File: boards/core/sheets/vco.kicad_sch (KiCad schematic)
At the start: 53 parts, among them Q201 2N3906, Q202 BC847BS, Q206 MMBFJ111, Q301 MMBT5551, U201 TL072, U202 TL072, U206 LM311

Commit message: Added schematics docs
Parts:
- renumbered C274 to C273, Q206 to Q203, R323 to R322, R325 to R324, R327 to R326, R331 to R330, TH204 to TH203, TP205 to TP201, TP206 to TP202, TP207 to TP203, TP208 to TP204, TP234 to TP233, U206 to U203
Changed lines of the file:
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@@
 		(dnp no)
 		(fields_autoplaced yes)
-		(property "Reference" "#PWR0381"
+		(property "Reference" "#PWR0380"
 			(at 43.18 87.63 0)
 			(effects
@@
 		(on_board yes)
 		(dnp no)
-		(property "Reference" "TP208"
+		(property "Reference" "TP204"
 			(at 279.4 46.99 90)
 			(effects
@@
 		(dnp no)
 		(fields_autoplaced yes)
-		(property "Reference" "C274"
+		(property "Reference" "C273"
 			(at 269.24 128.27 90)
 			(effects
@@
 		(dnp no)
 		(fields_autoplaced yes)
-		(property "Reference" "R325"
+		(property "Reference" "R324"
 			(at 237.49 144.78 0)
 			(effects
@@
 		(on_board yes)
 		(dnp no)
-		(property "Reference" "TP206"
+		(property "Reference" "TP202"
 			(at 158.115 134.62 90)
 			(effects
@@
 		(dnp no)
 		(fields_autoplaced yes)
-		(property "Reference" "#PWR0389"
+		(property "Reference" "#PWR0388"
 			(at 234.95 163.83 0)
 			(effects
@@
 		(on_board yes)
 		(dnp no)
-		(property "Reference" "TP207"
+		(property "Reference" "TP203"
 			(at 235.585 91.44 90)
 			(effects
@@
 		(on_board yes)
 		(dnp no)
-		(property "Reference" "U206"
+		(property "Reference" "U203"
 			(at 266.7 63.5 0)
 			(effects
@@
 		(dnp no)
 		(fields_autoplaced yes)
-		(property "Reference" "#PWR0385"
+		(property "Reference" "#PWR0384"
 			(at 219.71 154.94 0)
 			(effects
@@
 		(on_board yes)
 		(dnp no)
-		(property "Reference" "TP205"
+		(property "Reference" "TP201"
 			(at 148.59 57.15 0)
 			(effects
@@
 		(dnp no)
 		(fields_autoplaced yes)
-		(property "Reference" "#PWR0387"
+		(property "Reference" "#PWR0386"
 			(at 228.6 148.59 0)
 			(effects
@@
 		(dnp no)
 		(fields_autoplaced yes)
-		(property "Reference" "#PWR0383"
+		(property "Reference" "#PWR0382"
 			(at 43.18 96.52 0)
 			(effects
@@
 		(dnp no)
 		(fields_autoplaced yes)
-		(property "Reference" "#PWR0393"
+		(property "Reference" "#PWR0392"
 			(at 288.29 153.67 0)
 			(effects
@@
 		(dnp no)
 		(fields_autoplaced yes)
-		(property "Reference" "R327"
+		(property "Reference" "R326"
 			(at 237.49 154.94 0)
 			(effects
@@
 		(dnp no)
 		(fields_autoplaced yes)
-		(property "Reference" "TH204"
+		(property "Reference" "TH203"
 			(at 117.1575 71.12 90)
 			(effects
@@
 		(dnp no)
 		(fields_autoplaced yes)
-		(property "Reference" "#PWR0241"
+		(property "Reference" "#PWR0224"
 			(at 246.38 105.41 0)
 			(effects
@@
 		(dnp no)
 		(fields_autoplaced yes)
-		(property "Reference" "#PWR0391"
+		(property "Reference" "#PWR0390"
 			(at 274.32 153.67 0)
 			(effects
@@
 		(dnp no)
 		(fields_autoplaced yes)
-		(property "Reference" "#PWR0370"
+		(property "Reference" "#PWR0369"
 			(at 111.76 134.62 0)
 			(effects
@@
 		(dnp no)
 		(fields_autoplaced yes)
-		(property "Reference" "Q206"
+		(property "Reference" "Q203"
 			(at 224.79 41.91 90)
 			(effects
@@
 		(dnp no)
 		(fields_autoplaced yes)
-		(property "Reference" "R323"
+		(property "Reference" "R322"
 			(at 222.25 138.43 0)
 			(effects
@@
 		(dnp no)
 		(fields_autoplaced yes)
-		(property "Reference" "#PWR0244"
+		(property "Reference" "#PWR0227"
 			(at 271.78 83.82 0)
 			(effects
@@
 		(dnp no)
 		(fields_autoplaced yes)
-		(property "Reference" "R331"
+		(property "Reference" "R330"
 			(at 290.83 140.97 0)
 			(effects
@@
 		(on_board yes)
 		(dnp no)
-		(property "Reference" "TP234"
+		(property "Reference" "TP233"
 			(at 226.695 72.39 90)
 			(effects
@@
 		(dnp no)
 		(fields_autoplaced yes)
-		(property "Reference" "#PWR0240"
+		(property "Reference" "#PWR0223"
 			(at 246.38 82.55 0)
 			(effects
@@
 		(dnp no)
 		(fields_autoplaced yes)
-		(property "Reference" "#PWR0395"
+		(property "Reference" "#PWR0394"
 			(at 299.72 153.67 0)
 			(effects

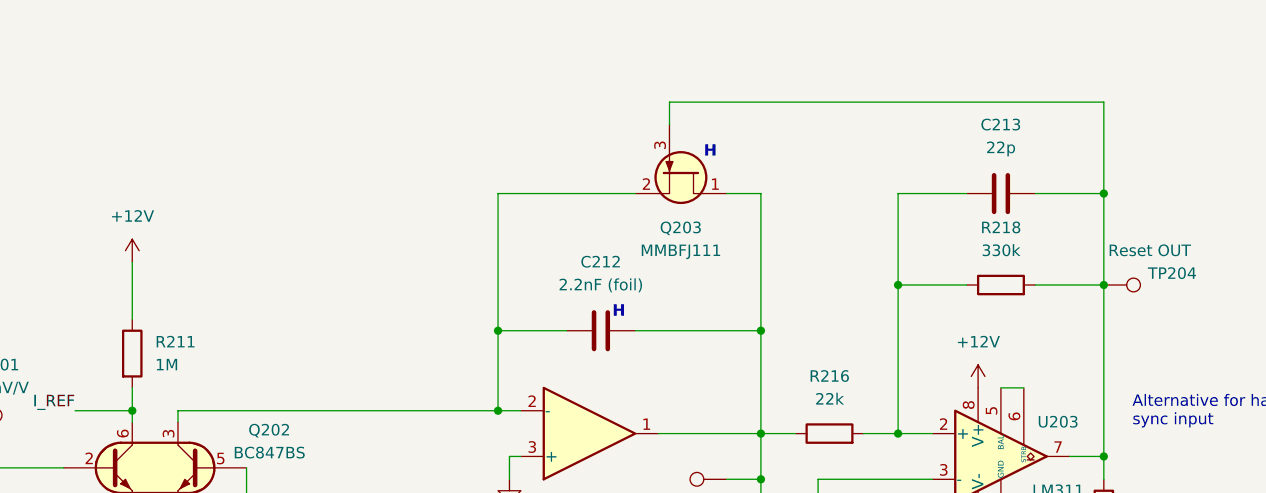
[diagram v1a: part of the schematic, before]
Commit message: Added THT footprint to J111 in VCOs
https://github.com/shmoergh/hog/issues/10
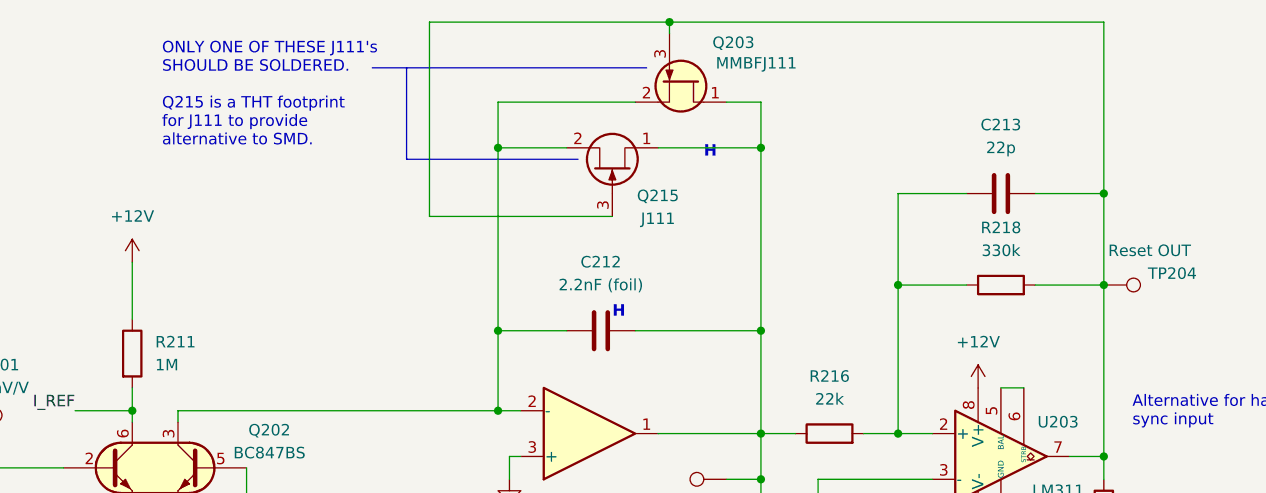
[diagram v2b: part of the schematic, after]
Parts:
- added Q215: J111, Package_TO_SOT_THT:TO-92_Inline_Wide, symbol Transistor_FET:MMBFJ111
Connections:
- net RAW_SAW: now also Q215.1 (D)
- net at C213.2, Q203.3 (G), R218.2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: now also Q215.3 (G)
- net at C212.1, Q202.3 (C2), Q203.2 (S)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: now also Q215.2 (S)
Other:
- note added: "ONLY ONE OF THESE J111's SHOULD BE SOLDERED. Q215 is a THT footprint for J111 to provide alternative to SMD."
- moved on the sheet: Q203
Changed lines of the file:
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@@
 	)
 	(junction
+		(at 223.52 19.05)
+		(diameter 0)
+		(color 0 0 0 0)
+	)
+	(junction
 		(at 60.96 66.04)
 		(diameter 0)
@@
 	)
 	(junction
+		(at 233.68 33.02)
+		(diameter 0)
+		(color 0 0 0 0)
+	)
+	(junction
 		(at 148.59 68.58)
 		(diameter 0)
@@
 	)
 	(junction
+		(at 204.47 33.02)
+		(diameter 0)
+		(color 0 0 0 0)
+	)
+	(junction
 		(at 288.29 135.89)
 		(diameter 0)
@@
 	(wire
 		(pts
-			(xy 233.68 38.1) (xy 233.68 53.34)
+			(xy 233.68 27.94) (xy 233.68 33.02)
 		)
 		(stroke
@@
 		)
 	)
+	(polyline
+		(pts
+			(xy 190.5 24.13) (xy 220.98 24.13)
+		)
+		(stroke
+			(width 0)
+			(type default)
+		)
+	)
 	(wire
 		(pts
@@
 	(wire
 		(pts
+			(xy 222.25 33.02) (xy 233.68 33.02)
+		)
+		(stroke
+			(width 0)
+			(type default)
+		)
+	)
+	(wire
+		(pts
 			(xy 128.27 128.27) (xy 128.27 130.81)
 		)
@@
 	(wire
 		(pts
+			(xy 196.85 40.64) (xy 196.85 19.05)
+		)
+		(stroke
+			(width 0)
+			(type default)
+		)
+	)
+	(wire
+		(pts
 			(xy 161.29 132.08) (xy 166.37 132.08)
 		)
@@
 	(wire
 		(pts
+			(xy 204.47 33.02) (xy 204.47 53.34)
+		)
+		(stroke
+			(width 0)
+			(type default)
+		)
+	)
+	(wire
+		(pts
 			(xy 233.68 69.85) (xy 233.68 81.28)
 		)
@@
 		)
 	)
+	(polyline
+		(pts
+			(xy 194.31 34.29) (xy 213.36 34.29)
+		)
+		(stroke
+			(width 0)
+			(type default)
+		)
+	)
 	(wire
 		(pts
@@
 	(wire
 		(pts
-			(xy 204.47 38.1) (xy 219.71 38.1)
+			(xy 204.47 27.94) (xy 219.71 27.94)
 		)
 		(stroke
@@
 		)
 	)
+	(polyline
+		(pts
+			(xy 194.31 24.13) (xy 194.31 34.29)
+		)
+		(stroke
+			(width 0)
+			(type default)
+		)
+	)
 	(wire
 		(pts
@@
 	(wire
 		(pts
-			(xy 223.52 27.94) (xy 223.52 30.48)
+			(xy 223.52 19.05) (xy 223.52 20.32)
 		)
 		(stroke
@@
 	(wire
 		(pts
+			(xy 217.17 40.64) (xy 196.85 40.64)
+		)
+		(stroke
+			(width 0)
+			(type default)
+		)
+	)
+	(wire
+		(pts
 			(xy 148.59 114.3) (xy 148.59 125.73)
 		)
@@
 	(wire
 		(pts
-			(xy 229.87 38.1) (xy 233.68 38.1)
+			(xy 229.87 27.94) (xy 233.68 27.94)
 		)
 		(stroke
@@
 	(wire
 		(pts
-			(xy 271.78 38.1) (xy 271.78 27.94)
+			(xy 271.78 38.1) (xy 271.78 19.05)
 		)
 		(stroke
@@
 	(wire
 		(pts
+			(xy 196.85 19.05) (xy 223.52 19.05)
+		)
+		(stroke
+			(width 0)
+			(type default)
+		)
+	)
+	(wire
+		(pts
 			(xy 148.59 125.73) (xy 149.86 125.73)
 		)
@@
 	(wire
 		(pts
-			(xy 204.47 38.1) (xy 204.47 53.34)
+			(xy 204.47 27.94) (xy 204.47 33.02)
 		)
 		(stroke
@@
 	(wire
 		(pts
+			(xy 204.47 33.02) (xy 212.09 33.02)
+		)
+		(stroke
+			(width 0)
+			(type default)
+		)
+	)
+	(wire
+		(pts
 			(xy 166.37 151.13) (xy 166.37 152.4)
 		)
@@
 	(wire
 		(pts
-			(xy 223.52 27.94) (xy 271.78 27.94)
+			(xy 223.52 19.05) (xy 271.78 19.05)
 		)
 		(stroke
@@
 	(wire
 		(pts
+			(xy 233.68 33.02) (xy 233.68 53.34)
+		)
+		(stroke
+			(width 0)
+			(type default)
+		)
+	)
+	(wire
+		(pts
 			(xy 157.48 62.23) (xy 163.83 62.23)
 		)
@@
 		)
 	)
+	(text "ONLY ONE OF THESE J111's\nSHOULD BE SOLDERED.\n\nQ215 is a THT footprint\nfor J111 to provide \nalternative to SMD."
+		(exclude_from_sim no)
+		(at 167.132 27.178 0)
+		(effects
+			(font
+				(size 1.27 1.27)
+			)
+			(justify left)
+		)
+	)
 	(text "H"
 		(exclude_from_sim no)
@@
 	)
 	(symbol
+		(lib_id "Transistor_FET:MMBFJ111")
+		(at 217.17 35.56 270)
+		(mirror x)
+		(unit 1)
+		(exclude_from_sim no)
+		(in_bom no)
+		(on_board yes)
+		(dnp no)
+		(property "Reference" "Q215"
+			(at 222.25 38.354 90)
+			(effects
+				(font
+					(size 1.27 1.27)
+				)
+			)
+		)
+		(property "Value" "J111"
+			(at 222.25 40.894 90)
+			(effects
+				(font
+					(size 1.27 1.27)
+				)
+			)
+		)
+		(property "Footprint" "Package_TO_SOT_THT:TO-92_Inline_Wide"
+			(at 215.265 30.48 0)
+			(effects
+				(font
+					(size 1.27 1.27)
+					(italic yes)
+				)
+				(justify left)
+				(hide yes)
+			)
+		)
+		(property "Datasheet" ""
+			(at 213.36 30.48 0)
+			(effects
+				(font
+					(size 1.27 1.27)
+				)
+				(justify left)
+				(hide yes)
+			)
+		)
+		(property "Description" ""
+			(at 217.17 35.56 0)
+			(effects
+				(font
+					(size 1.27 1.27)
+				)
+				(hide yes)
+			)
+		)
+		(property "Mouser" "512-J111"
+			(at 217.17 35.56 90)
+			(effects
+				(font
+					(size 1.27 1.27)
+				)
+				(hide yes)
+			)
+		)
+		(pin "1"
+		)
+		(pin "3"
+		)
+		(pin "2"
+		)
+		(instances
+			(project ""
+				(path "/91ae1fff-f2ac-4868-8c3f-8c5c03d8b2f6/031e86a6-ca4d-4816-ba7e-c07cacc1df65"
+					(reference "Q211")
+					(unit 1)
+				)
+				(path "/91ae1fff-f2ac-4868-8c3f-8c5c03d8b2f6/24bddecc-79ff-4d9f-8d29-90298f4415a6"
+					(reference "Q215")
+					(unit 1)
+				)
+			)
+		)
+	)
+	(symbol
 		(lib_id "Device:R")
 		(at 116.84 68.58 90)
@@
 	(symbol
 		(lib_id "PCM_Transistor_JFET_AKL:MMBFJ111")
-		(at 224.79 35.56 270)
+		(at 224.79 25.4 270)
 		(unit 1)
 		(exclude_from_sim no)
@@
 		(on_board yes)
 		(dnp no)
-		(fields_autoplaced yes)
 		(property "Reference" "Q203"
-			(at 224.79 41.91 90)
+			(at 230.632 21.336 90)
 			(effects
 				(font
@@
 		)
 		(property "Value" "MMBFJ111"
-			(at 224.79 44.45 90)
+			(at 233.172 23.622 90)
 			(effects
 				(font
@@
 		)
 		(property "Footprint" "PCM_Package_TO_SOT_SMD_AKL:SOT-23_Handsoldering"
-			(at 227.33 40.64 0)
+			(at 227.33 30.48 0)
 			(effects
 				(font
@@
 		)
 		(property "Datasheet" "https://www.tme.eu/Document/2ab8d7a6d6d8a209f9d7deeb52763e9f/J111.pdf"
-			(at 223.52 35.56 0)
+			(at 223.52 25.4 0)
 			(effects
 				(font
@@
 		)
 		(property "Description" ""
-			(at 224.79 35.56 0)
+			(at 224.79 25.4 0)
 			(effects
 				(font
@@
 		)
 		(property "LCSC" "C274688"
-			(at 224.79 35.56 90)
+			(at 224.79 25.4 90)
 			(effects
 				(font
